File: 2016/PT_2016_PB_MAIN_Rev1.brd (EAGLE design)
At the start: 150.9 x 201.9 mm, 127 parts, among them Q1 Q_IRFS7437PbF, Q11 Q_IRFS7437PbF, Q12 2N7002, Q14 Q_IRFS7437PbF, Q16 Q_IRFS7437PbF, Q2 2N7002, Q20 Q_IRFS7437PbF, Q6 Q_IRFS7437PbF, Q7 Q_IRFS7437PbF, Q9 Q_IRFS7437PbF

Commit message: Added Anderson Powerpole connectors, rerouted
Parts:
- removed 12V-AUX, 5V-AUX, AUX_P, AUX_P2, MOTOR_1, MOTOR_2, MOTOR_3, MOTOR_4, MOTOR_5, MOTOR_6: H_20020618-M02VERT, MRDT-2015-PowerBoard:20020620-M02
- added U$25, U$26, U$27, U$28, U$29, U$30, U$31, U$32, U$33, U$34, U$35, U$36, U$37, U$38, U$39, U$40: ANDERSON_POWERPOLEPP45_PCB_HORIZ_RIGHT, MRDT-Connectors:PP45_PCB_HORIZ_RIGHT
- added U$41, U$42, U$43, U$44: ANDERSON_POWERPOLEPP45_PCB_VERT, MRDT-Connectors:PP45_PCB_VERT
- moved LED3 2.03 mm to (142.0, 11.4)
- moved R8 2.03 mm to (134.6, 11.4)
- moved LED6 0.51 mm to (20.1, 18.0)
- moved R16 0.51 mm to (16.5, 19.3)
- moved LED10 0.25 mm to (20.1, 83.3)
- moved LED11 0.25 mm to (20.1, 116.3)
- moved R20 0.25 mm to (16.5, 51.6)
- moved R24 0.25 mm to (16.5, 84.6)
- moved R28 0.25 mm to (16.5, 101.1)
- moved LED1 0.25 mm to (20.1, 0.76)
- moved R9 0.25 mm to (16.5, 2.03)
- moved LED8 0.25 mm to (20.1, 50.3)
- moved LED12 0.25 mm to (20.1, 99.8)
- moved LED9 0.25 mm to (20.1, 66.8)
- moved R22 0.25 mm to (16.5, 68.1)
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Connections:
- net 12V-AUX: now also U$42.P$1; no longer 12V-AUX.R1, 12V-AUX.R2
- net 5V-AUX: now also U$44.P$1; no longer 5V-AUX.R1, 5V-AUX.R2
- net GND: now also U$25.P$1, U$27.P$1, U$29.P$1, U$31.P$1, U$33.P$1, U$35.P$1, U$37.P$1, U$39.P$1, U$41.P$1, U$43.P$1; no longer 12V-AUX.L1, 12V-AUX.L2, 5V-AUX.L1, 5V-AUX.L2, AUX_P.L1, AUX_P.L2, AUX_P2.L1, AUX_P2.L2, MOTOR_1.L1, MOTOR_1.L2, MOTOR_2.L1, MOTOR_2.L2, MOTOR_3.L1, MOTOR_3.L2, MOTOR_4.L1, MOTOR_4.L2, MOTOR_5.L1, MOTOR_5.L2, MOTOR_6.L1, MOTOR_6.L2
- net N$10: now also U$26.P$1; no longer AUX_P2.R1, AUX_P2.R2
- net N$29: now also U$38.P$1; no longer MOTOR_2.R1, MOTOR_2.R2
- net N$41: now also U$40.P$1; no longer MOTOR_1.R1, MOTOR_1.R2
- net N$45: now also U$32.P$1; no longer MOTOR_3.R1, MOTOR_3.R2
- net N$55: now also U$34.P$1; no longer MOTOR_4.R1, MOTOR_4.R2
- net N$61: now also U$28.P$1; no longer MOTOR_5.R1, MOTOR_5.R2
- net N$67: now also U$36.P$1; no longer MOTOR_6.R1, MOTOR_6.R2
- net N$79: now also U$30.P$1; no longer AUX_P.R1, AUX_P.R2
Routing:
- net 12V-AUX: track 10.0 -> 16.8 mm
- net AUX_P-IMEAS: track 173.4 -> 169.8 mm, vias 1 -> 2
- net M4-SIG: track 181.2 -> 177.9 mm
- net M3-SIG: track 202.3 -> 205.2 mm
- net M5-SIG: track 164.5 -> 162.0 mm
- net AUX_P2-IMEAS: track 159.6 -> 157.2 mm
- net 5V-AUX: track 15.0 -> 17.3 mm
- net M2-SIG: track 229.9 -> 232.1 mm
- net GND: track 138.9 -> 136.9 mm
- net M1-SIG: track 251.4 -> 253.2 mm
- net M5-IMEAS: track 204.8 -> 206.4 mm
- net M6-IMEAS: track 189.9 -> 191.2 mm
- net AUX_P-SIG: track 123.8 -> 122.5 mm
- net M6-SIG: track 141.2 -> 140.1 mm
- net M4-IMEAS: track 224.7 -> 225.5 mm
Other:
- board text added: "+"
- board text added: "+12V"
- board text added: "+5V"
- board text added: "GND"

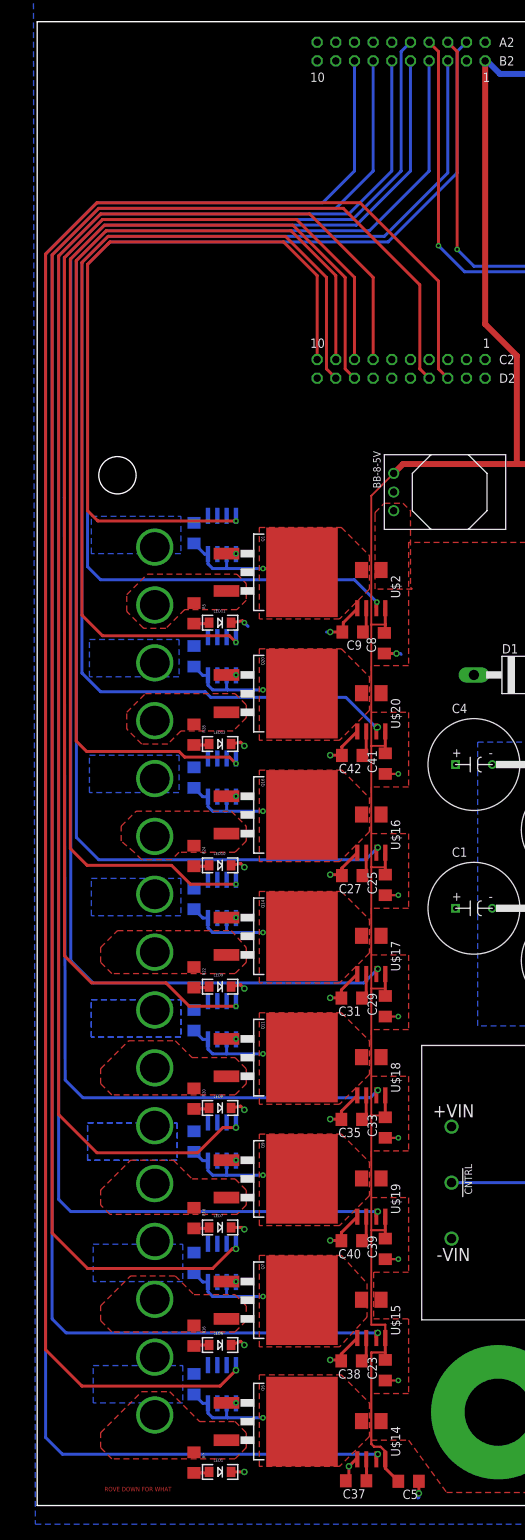
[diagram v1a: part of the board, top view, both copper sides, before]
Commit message: Added Mounting Holes
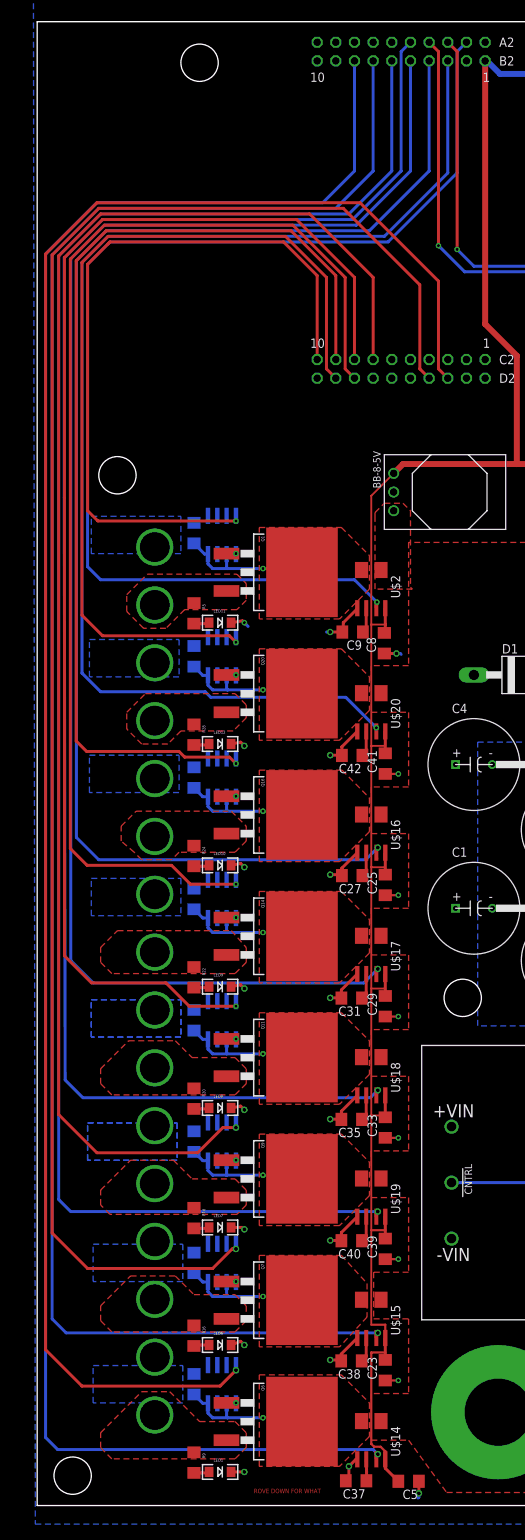
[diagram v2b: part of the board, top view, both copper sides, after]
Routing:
- net AUX_P-IMEAS: track 169.8 -> 169.6 mm, vias 2 -> 1
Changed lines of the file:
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@@
 <plain>
 <hole x="140.97" y="0.508" drill="5.08"/>
-<text x="13.462" y="-1.27" size="0.6096" layer="1" rot="R180">ROVE DOWN FOR WHAT</text>
+<text x="33.782" y="-1.524" size="0.6096" layer="1" rot="R180">ROVE DOWN FOR WHAT</text>
 <text x="123.698" y="7.112" size="1.6764" layer="21" rot="R180" align="bottom-center">Missouri S&amp;T Mars Rover
 Design Team
@@
 <text x="144.272" y="16.51" size="1.27" layer="21" rot="R90">GND</text>
 <text x="144.272" y="38.608" size="1.27" layer="21" rot="R90">GND</text>
+<hole x="0" y="0.254" drill="5.08"/>
+<hole x="53.086" y="65.278" drill="5.08"/>
+<hole x="17.272" y="192.532" drill="5.08"/>
 </plain>
 <attributes>
@@
 <contactref element="U$20" pad="7"/>
 <wire x1="41.3258" y1="101.54" x2="41.3258" y2="102.0318" width="0.4064" layer="1"/>
-<wire x1="41.3258" y1="102.0318" x2="41.529" y2="102.108" width="0.4064" layer="1"/>
-<via x="41.529" y="102.108" extent="1-16" drill="0.5"/>
 <wire x1="1.27" y1="109.474" x2="1.27" y2="165.354" width="0.4064" layer="16"/>
 <wire x1="42.418" y1="168.91" x2="4.826" y2="168.91" width="0.4064" layer="16"/>
@@
 <wire x1="41.3258" y1="3.1242" x2="41.529" y2="3.175" width="0.4064" layer="1"/>
 <via x="41.529" y="3.175" extent="1-16" drill="0.5"/>
-<wire x1="41.529" y1="3.175" x2="-1.397" y2="3.175" width="0.4064" layer="16"/>
-<wire x1="-1.397" y1="3.175" x2="-3.683" y2="5.461" width="0.4064" layer="16"/>
 <wire x1="-3.683" y1="5.461" x2="-3.683" y2="166.497" width="0.4064" layer="16"/>
 <wire x1="-3.683" y1="166.497" x2="3.302" y2="173.482" width="0.4064" layer="16"/>
@@
 <wire x1="34.036" y1="173.482" x2="38.354" y2="177.8" width="0.4064" layer="16"/>
 <wire x1="38.354" y1="177.8" x2="38.354" y2="192.786" width="0.4064" layer="16"/>
+<wire x1="-3.683" y1="5.461" x2="-2.032" y2="3.81" width="0.4064" layer="16"/>
+<wire x1="-2.032" y1="3.81" x2="40.894" y2="3.81" width="0.4064" layer="16"/>
+<wire x1="40.894" y1="3.81" x2="41.529" y2="3.175" width="0.4064" layer="16"/>
 </signal>
 <signal name="N$39">

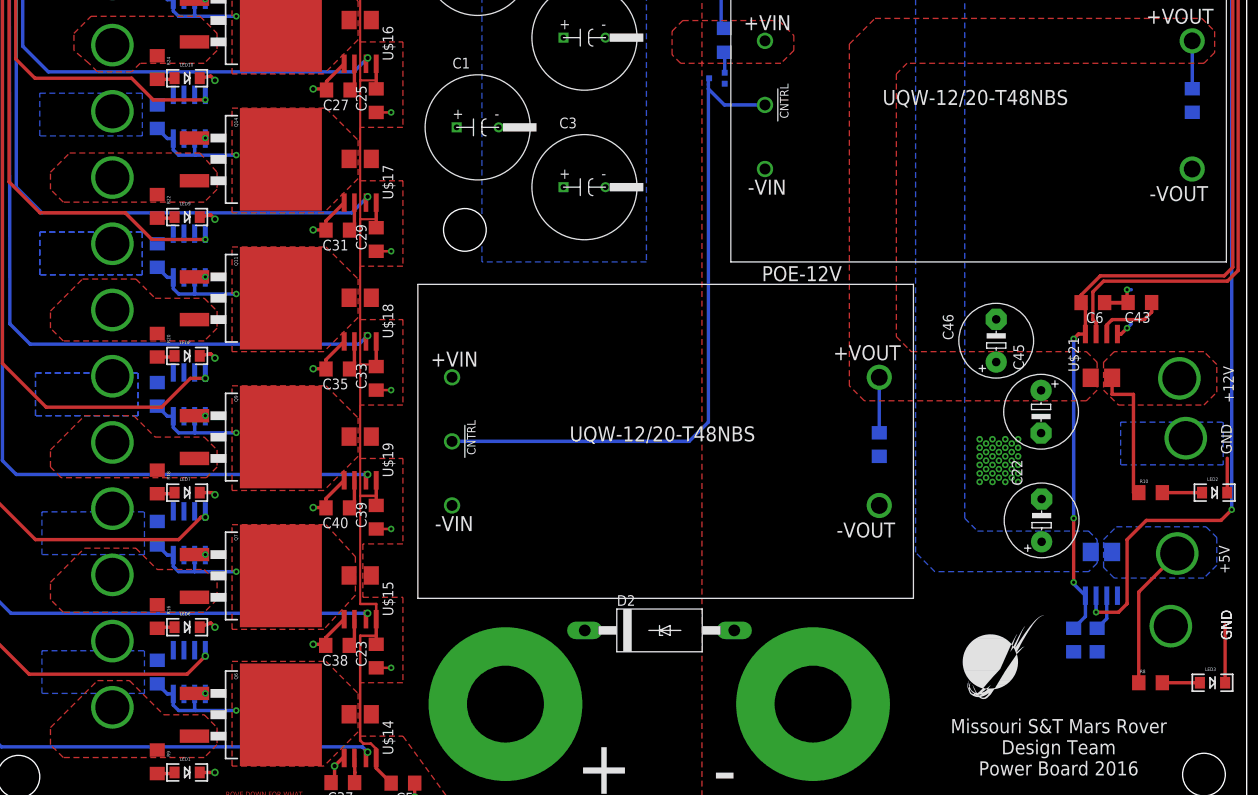
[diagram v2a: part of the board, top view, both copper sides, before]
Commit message: Swapped Individual APP terminals for 2-pos.
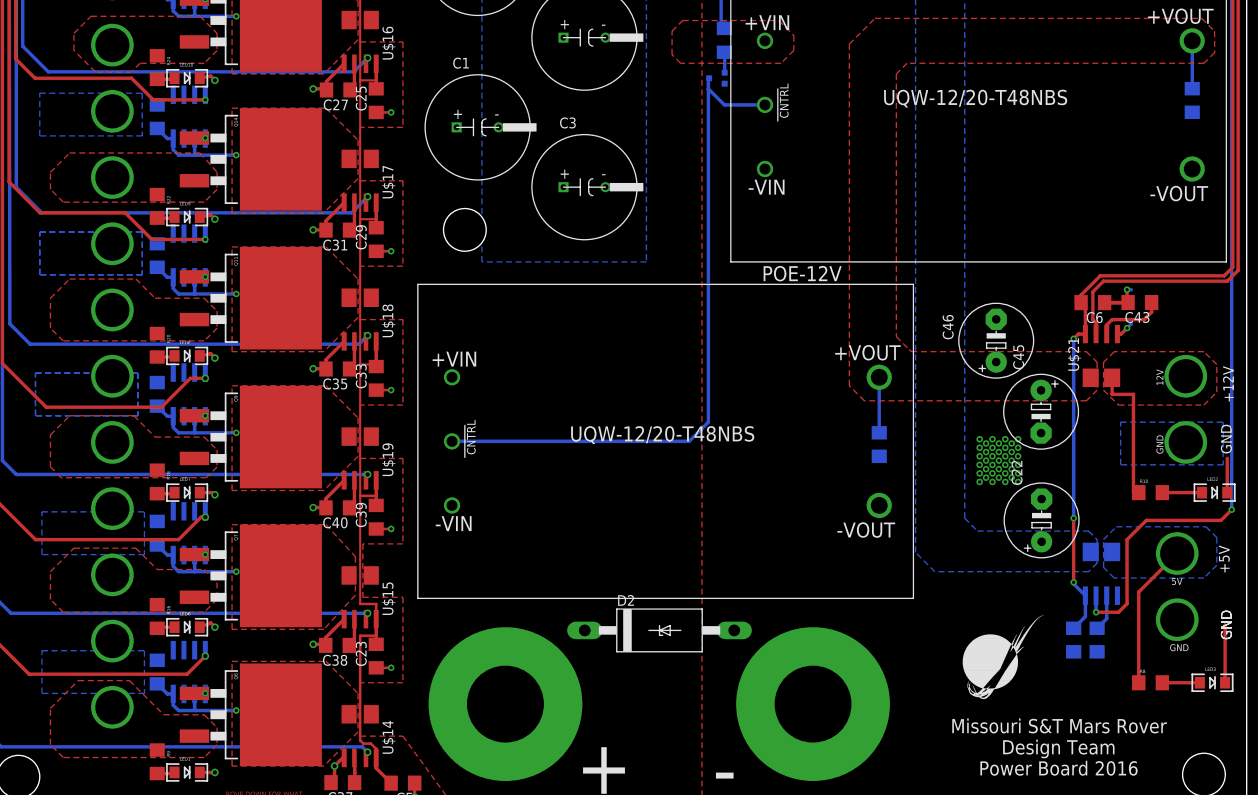
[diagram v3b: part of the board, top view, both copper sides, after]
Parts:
- removed U$41, U$42, U$43, U$44: ANDERSON_POWERPOLEPP45_PCB_VERT, MRDT-Connectors:PP45_PCB_VERT
- added U$45: APP_2POS_CONFIG5V_VERT, MRDT-Connectors:APP_5V_VERT_CONFIG
- added U$46: APP_2POS_CONFIG12V_VERT, MRDT-Connectors:APP_12V_VERT_CONFIG
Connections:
- net 12V-AUX: now also U$46.VCC; no longer U$42.P$1
- net 5V-AUX: now also U$45.VCC; no longer U$44.P$1
- net GND: now also U$45.GND, U$46.GND; no longer U$41.P$1, U$43.P$1
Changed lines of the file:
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@@
 <element name="U$39" library="MRDT-Connectors" package="PP45_PCB_HORIZ_RIGHT" value="ANDERSON_POWERPOLEPP45_PCB_HORIZ_RIGHT" x="-17.018" y="28.194"/>
 <element name="U$40" library="MRDT-Connectors" package="PP45_PCB_HORIZ_RIGHT" value="ANDERSON_POWERPOLEPP45_PCB_HORIZ_RIGHT" x="-17.018" y="4.572"/>
-<element name="U$41" library="MRDT-Connectors" package="PP45_PCB_VERT" value="ANDERSON_POWERPOLEPP45_PCB_VERT" x="141.986" y="36.576" rot="R90"/>
-<element name="U$42" library="MRDT-Connectors" package="PP45_PCB_VERT" value="ANDERSON_POWERPOLEPP45_PCB_VERT" x="134.112" y="44.45"/>
-<element name="U$43" library="MRDT-Connectors" package="PP45_PCB_VERT" value="ANDERSON_POWERPOLEPP45_PCB_VERT" x="133.858" y="22.098" rot="R270"/>
-<element name="U$44" library="MRDT-Connectors" package="PP45_PCB_VERT" value="ANDERSON_POWERPOLEPP45_PCB_VERT" x="141.732" y="29.972" rot="R180"/>
+<element name="U$45" library="MRDT-Connectors" package="APP_5V_VERT_CONFIG" value="APP_2POS_CONFIG5V_VERT" x="133.858" y="14.224"/>
+<element name="U$46" library="MRDT-Connectors" package="APP_12V_VERT_CONFIG" value="APP_2POS_CONFIG12V_VERT" x="134.112" y="36.068"/>
 </elements>
 <signals>
@@
 <vertex x="-12.954" y="-12.954"/>
 </polygon>
-<contactref element="U$41" pad="P$1"/>
-<contactref element="U$43" pad="P$1"/>
 <contactref element="U$35" pad="P$1"/>
+<contactref element="U$46" pad="GND"/>
+<contactref element="U$45" pad="GND"/>
 </signal>
 <signal name="V_BATT">
@@
 <contactref element="U$21" pad="4"/>
 <contactref element="R10" pad="1"/>
-<contactref element="U$42" pad="P$1"/>
 <polygon width="0.4064" layer="1" thermals="no">
 <vertex x="129.032" y="49.53"/>
@@
 <wire x1="132.588" y1="45.72" x2="130.048" y2="45.72" width="0.4064" layer="1"/>
 <wire x1="130.048" y1="45.72" x2="130.048" y2="47.692" width="0.4064" layer="1"/>
+<contactref element="U$46" pad="VCC"/>
 </signal>
 <signal name="N$40">
@@
 <polygon width="0.4064" layer="1" thermals="no">
 <vertex x="3.81" y="4.064"/>
-<vertex x="3.81" y="6.096"/>
-<vertex x="9.398" y="11.684"/>
+<vertex x="3.81" y="8.382"/>
+<vertex x="7.112" y="11.684"/>
 <vertex x="13.208" y="11.684"/>
 <vertex x="17.272" y="7.62"/>
@@
 <polygon width="0.4064" layer="1" thermals="no">
 <vertex x="3.81" y="21.336"/>
-<vertex x="3.81" y="23.368"/>
-<vertex x="7.874" y="27.432"/>
+<vertex x="3.81" y="24.638"/>
+<vertex x="6.604" y="27.432"/>
 <vertex x="13.97" y="27.432"/>
 <vertex x="16.51" y="24.892"/>
@@
 <polygon width="0.4064" layer="1" thermals="no">
 <vertex x="3.81" y="37.084"/>
-<vertex x="3.81" y="39.116"/>
-<vertex x="7.874" y="43.18"/>
+<vertex x="3.81" y="40.894"/>
+<vertex x="6.096" y="43.18"/>
 <vertex x="13.716" y="43.18"/>
 <vertex x="16.256" y="40.64"/>
@@
 <polygon width="0.4064" layer="1" thermals="no">
 <vertex x="3.81" y="53.594"/>
-<vertex x="3.81" y="55.626"/>
-<vertex x="7.62" y="59.436"/>
+<vertex x="3.81" y="57.15"/>
+<vertex x="6.096" y="59.436"/>
 <vertex x="13.97" y="59.436"/>
 <vertex x="16.256" y="57.15"/>
@@
 <vertex x="14.478" y="85.09"/>
 <vertex x="13.462" y="84.074"/>
-<vertex x="9.398" y="84.074"/>
-<vertex x="8.382" y="85.09"/>
+<vertex x="9.144" y="84.074"/>
 </polygon>
 <contactref element="U$36" pad="P$1"/>
@@
 <contactref element="R8" pad="1"/>
 <contactref element="U$3" pad="4"/>
-<contactref element="U$44" pad="P$1"/>
 <polygon width="0.4064" layer="16" thermals="no">
 <vertex x="142.494" y="28.702"/>
@@
 </polygon>
 <wire x1="133.22" y1="11.43" x2="133.22" y2="22.222" width="0.4064" layer="1"/>
+<contactref element="U$45" pad="VCC"/>
 <wire x1="133.22" y1="22.222" x2="137.795" y2="26.797" width="0.4064" layer="1"/>
 </signal>
